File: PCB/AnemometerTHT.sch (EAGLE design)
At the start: 36 parts, among them IC1 TINY2313A, IC2 74HC151D, IC3 74HC151D, IC4 74HC08D, IC5 LM555N, IC6 74HC138D, IC7 74CH14D, IC8 74HC393D, Q1 16MHz

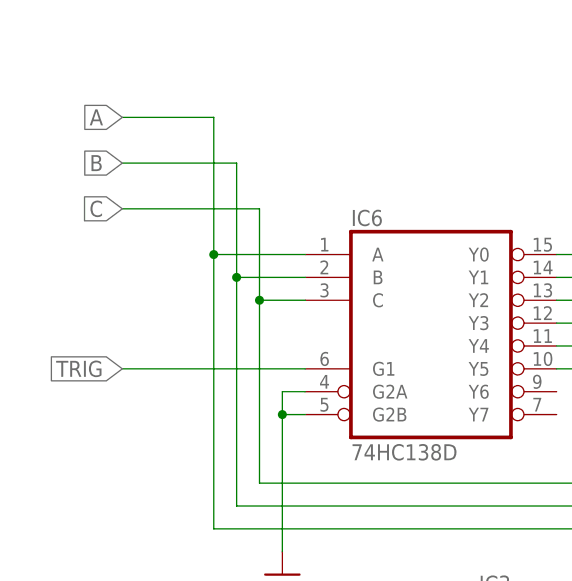
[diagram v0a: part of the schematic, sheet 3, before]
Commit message: realized that i inverted the wrong signal
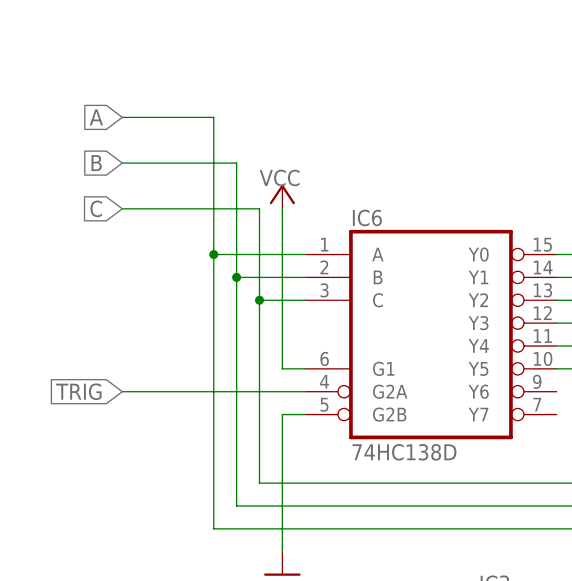
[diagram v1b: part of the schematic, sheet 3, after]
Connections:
- net GND: no longer IC6A.G2A
- net TRIG: now also IC6A.G2A; no longer IC6A.G1
- net VCC: now also IC6A.G1
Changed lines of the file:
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@@
 <part name="GND20" library="supply1" library_urn="urn:adsk.eagle:library:371" deviceset="GND" device=""/>
 <part name="P+13" library="supply1" library_urn="urn:adsk.eagle:library:371" deviceset="VCC" device=""/>
+<part name="P+14" library="supply1" library_urn="urn:adsk.eagle:library:371" deviceset="VCC" device=""/>
 </parts>
 <sheets>
@@
 <attribute name="VALUE" x="101.6" y="12.7" size="1.778" layer="96" rot="MR0"/>
 </instance>
+<instance part="P+14" gate="VCC" x="43.18" y="139.7" smashed="yes">
+<attribute name="VALUE" x="40.64" y="139.7" size="1.778" layer="96"/>
+</instance>
 </instances>
 <busses>
@@
 <net name="TRIG" class="0">
 <segment>
-<pinref part="IC6" gate="A" pin="G1"/>
-<wire x1="45.72" y1="119.38" x2="25.4" y2="119.38" width="0.1524" layer="91"/>
-<label x="25.4" y="119.38" size="1.778" layer="95" rot="R180" xref="yes"/>
+<label x="25.4" y="116.84" size="1.778" layer="95" rot="R180" xref="yes"/>
+<pinref part="IC6" gate="A" pin="G2A"/>
+<wire x1="45.72" y1="116.84" x2="25.4" y2="116.84" width="0.1524" layer="91"/>
 </segment>
 </net>
@@
 <wire x1="43.18" y1="99.06" x2="43.18" y2="114.3" width="0.1524" layer="91"/>
 <wire x1="43.18" y1="114.3" x2="45.72" y2="114.3" width="0.1524" layer="91"/>
-<pinref part="IC6" gate="A" pin="G2A"/>
-<wire x1="45.72" y1="116.84" x2="43.18" y2="116.84" width="0.1524" layer="91"/>
-<wire x1="43.18" y1="116.84" x2="43.18" y2="114.3" width="0.1524" layer="91"/>
-<junction x="43.18" y="114.3"/>
 </segment>
 <segment>
@@
 <wire x1="236.22" y1="149.86" x2="233.68" y2="149.86" width="0.1524" layer="91"/>
 </segment>
-</net>
+<segment>
+<pinref part="IC6" gate="A" pin="G1"/>
+<pinref part="P+14" gate="VCC" pin="VCC"/>
+<wire x1="45.72" y1="119.38" x2="43.18" y2="119.38" width="0.1524" layer="91"/>
+<wire x1="43.18" y1="119.38" x2="43.18" y2="137.16" width="0.1524" layer="91"/>
+</segment>
+</net>

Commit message: added offset corection
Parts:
- added R9: 10k, rcl:R-EU_0204/7
- added S1, S2: (no value), switch-omron:10-XX
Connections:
- new net SET0: IC1.(OC1B)PB4, R9.1, S2.S, S2.S1
- net GND: now also S1.P, S1.P1, S2.P, S2.P1
- net RST: now also S1.S, S1.S1
- net VCC: now also R9.2

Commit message: moved puls counter to in/4
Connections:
- new net PULS*4: IC1.(T0)PD4, IC8A.QA
- net PULS: now also IC8A.QC; no longer IC8A.QB
- net PULS*2: now also IC1.(INT0)PD2, IC8A.QB; no longer IC1.(T0)PD4, IC8A.QA
